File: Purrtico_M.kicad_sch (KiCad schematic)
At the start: 119 parts, among them J1 Conn_02x05_Odd_Even, J2 Conn_01x02, J4 Conn_01x02, U1 OPA1679, U2 OPA1679, U3 OPA1679

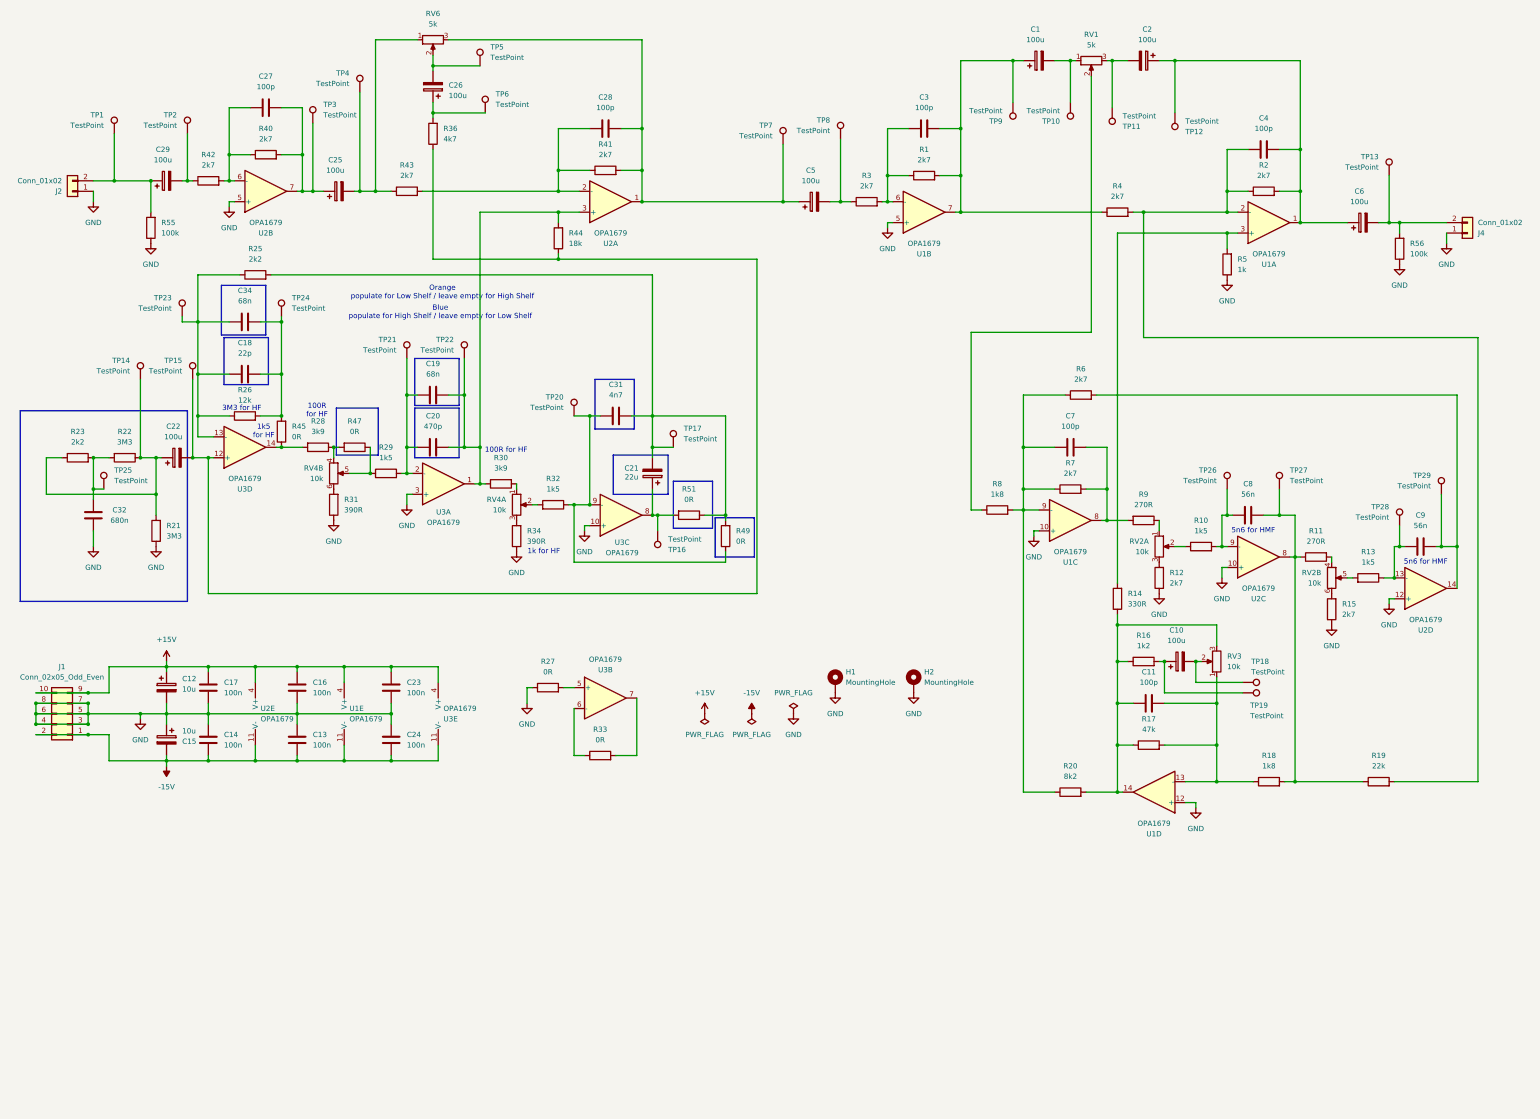
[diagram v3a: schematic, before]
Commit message: update pcb
swapped potentiometer pinouts, increased potentiometer spacing on pcb
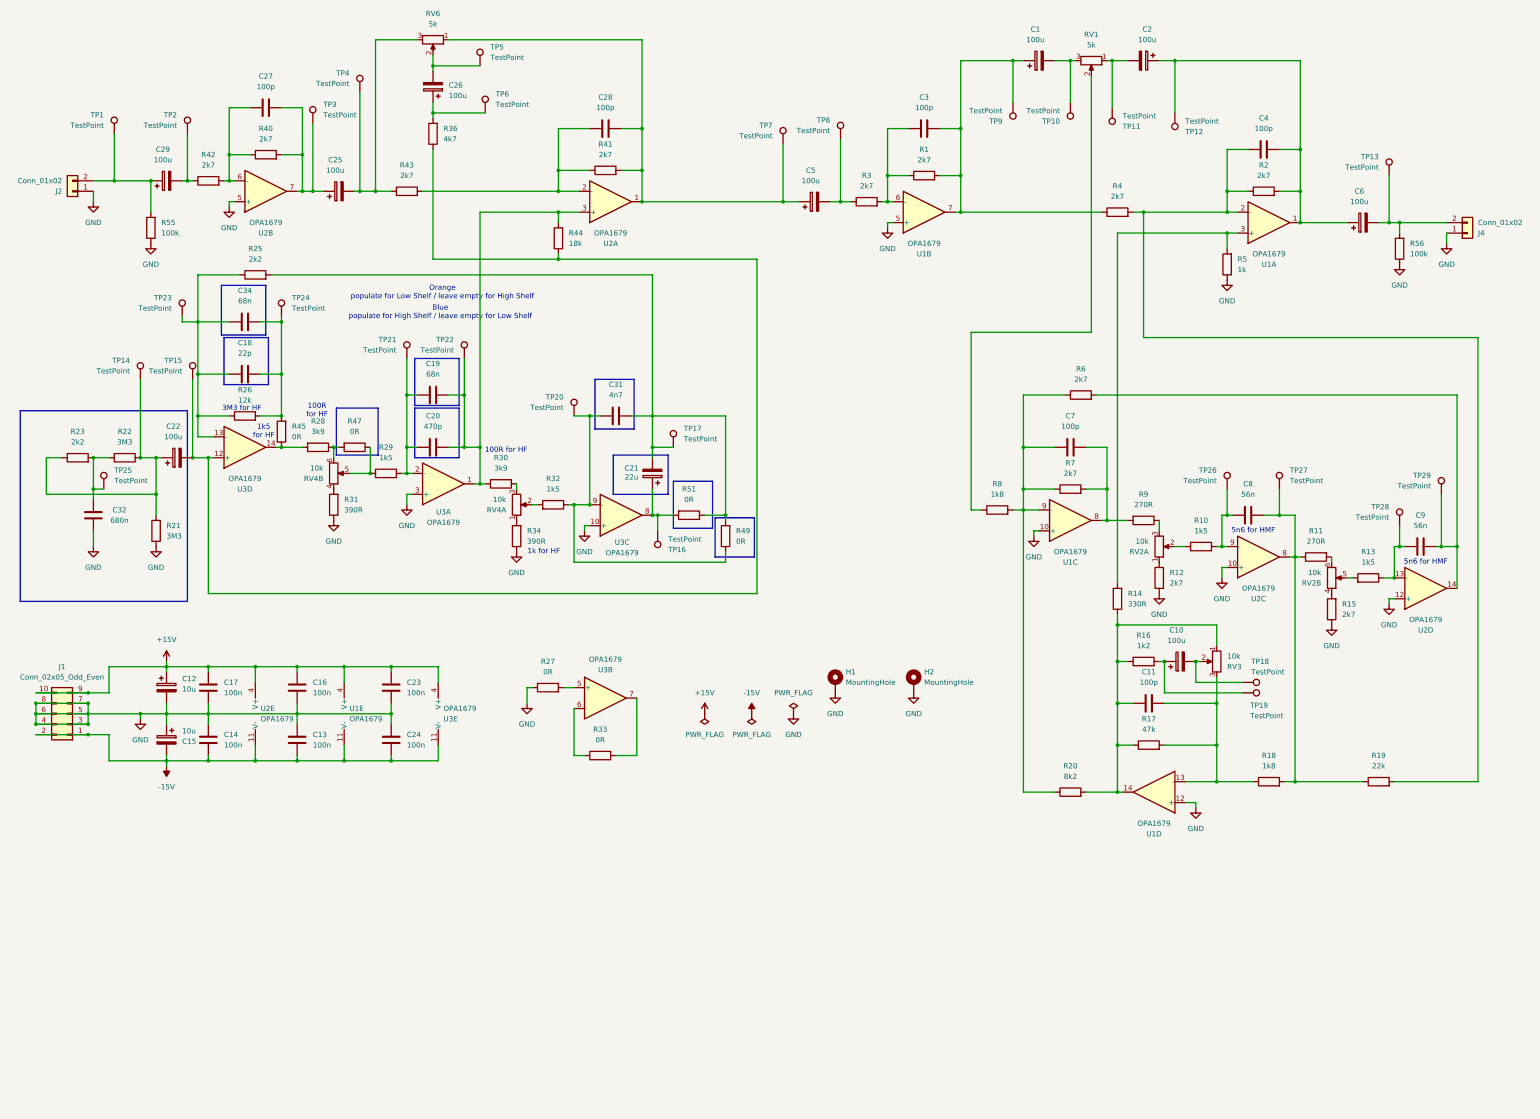
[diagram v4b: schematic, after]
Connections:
- net at C1.2, TP10.1: now also RV1.3; no longer RV1.1
- net at C2.2, TP11.1: now also RV1.1; no longer RV1.3
- net at C25.2, R43.1, TP4.1: now also RV6.3; no longer RV6.1
- net at C28.2, C5.1, R41.2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: now also RV6.1; no longer RV6.3
- net at C11.1, R14.1, R16.1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: now also RV3.1; no longer RV3.3
- net at C11.2, R17.2, R18.1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: now also RV3.3; no longer RV3.1
- net at R9.1: now also RV2.3; no longer RV2.1
- net at R28.1, R47.2: now also RV4.6; no longer RV4.4
- net at R31.2: now also RV4.4; no longer RV4.6
- net at R11.2: now also RV2.6; no longer RV2.4
- net at R12.2: now also RV2.1; no longer RV2.3
- net at R15.2: now also RV2.4; no longer RV2.6
- net at R34.2: now also RV4.1; no longer RV4.3
- net at R30.2: now also RV4.3; no longer RV4.1
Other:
- moved on the sheet: RV1, RV3, RV6
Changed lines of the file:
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@@
 	(symbol
 		(lib_id "Device:R_Potentiometer")
-		(at 295.91 27.94 90)
-		(mirror x)
+		(at 295.91 27.94 270)
 		(unit 1)
 		(exclude_from_sim no)
@@
 		(on_board yes)
 		(dnp no)
-		(fields_autoplaced yes)
 		(property "Reference" "RV1"
 			(at 295.91 21.59 90)
@@
 	(symbol
 		(lib_id "Device:R_Potentiometer")
-		(at 135.89 22.86 90)
-		(mirror x)
+		(at 135.89 22.86 270)
 		(unit 1)
 		(exclude_from_sim no)
@@
 		(on_board yes)
 		(dnp no)
-		(fields_autoplaced yes)
 		(property "Reference" "RV6"
 			(at 135.89 16.51 90)
@@
 		(lib_id "Device:R_Potentiometer_Dual_Separate")
 		(at 111.76 128.27 0)
+		(mirror x)
 		(unit 2)
 		(exclude_from_sim no)
@@
 		(dnp no)
 		(property "Reference" "RV4"
-			(at 109.22 126.9999 0)
+			(at 109.22 129.5401 0)
 			(effects
 				(font
@@
 		)
 		(property "Value" "10k"
-			(at 109.22 129.5399 0)
+			(at 109.22 127.0001 0)
 			(effects
 				(font
@@
 		(lib_id "Device:R_Potentiometer_Dual_Separate")
 		(at 312.42 146.05 0)
+		(mirror x)
 		(unit 1)
 		(exclude_from_sim no)
@@
 		(on_board yes)
 		(dnp no)
-		(fields_autoplaced yes)
 		(property "Reference" "RV2"
-			(at 309.88 144.7799 0)
+			(at 309.88 147.3201 0)
 			(effects
 				(font
@@
 		)
 		(property "Value" "10k"
-			(at 309.88 147.3199 0)
+			(at 309.88 144.7801 0)
 			(effects
 				(font
@@
 		(lib_id "Device:R_Potentiometer_Dual_Separate")
 		(at 354.33 153.67 0)
+		(mirror x)
 		(unit 2)
 		(exclude_from_sim no)
@@
 		(dnp no)
 		(property "Reference" "RV2"
-			(at 351.79 152.3999 0)
+			(at 351.79 154.9401 0)
 			(effects
 				(font
@@
 		)
 		(property "Value" "10k"
-			(at 351.79 154.9399 0)
+			(at 351.79 152.4001 0)
 			(effects
 				(font
@@
 		(lib_id "Device:R_Potentiometer_Dual_Separate")
 		(at 156.21 135.89 0)
+		(mirror x)
 		(unit 1)
 		(exclude_from_sim no)
@@
 		(on_board yes)
 		(dnp no)
-		(fields_autoplaced yes)
 		(property "Reference" "RV4"
-			(at 153.67 134.6199 0)
+			(at 153.67 137.1601 0)
 			(effects
 				(font
@@
 		)
 		(property "Value" "10k"
-			(at 153.67 137.1599 0)
+			(at 153.67 134.6201 0)
 			(effects
 				(font
@@
 	(symbol
 		(lib_id "Device:R_Potentiometer")
-		(at 326.39 173.99 180)
+		(at 326.39 173.99 0)
+		(mirror y)
 		(unit 1)
 		(exclude_from_sim no)
@@
 		(on_board yes)
 		(dnp no)
-		(fields_autoplaced yes)
 		(property "Reference" "RV3"
-			(at 328.93 172.7199 0)
+			(at 328.93 175.2601 0)
 			(effects
 				(font
@@
 		)
 		(property "Value" "10k"
-			(at 328.93 175.2599 0)
+			(at 328.93 172.7201 0)
 			(effects
 				(font

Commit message: clean up pcb
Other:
- title: Purrtico M EQ -> Purrtico M
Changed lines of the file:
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@@
 	(paper "A3")
 	(title_block
-		(title "Purrtico M EQ")
-		(date "2024-07-31")
+		(title "Purrtico M")
+		(date "2024-08-02")
 		(rev "01")
 		(company "Greybox Audio")

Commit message: tweak LF EQ
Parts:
- C19: value 68n -> 100n
- C32: value 680n -> 1u
- R23: value 2k2 -> 1k
- R28, R30: value 3k9 -> 100R
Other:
- note removed: "100R for HF"
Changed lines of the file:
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@@
 	(title_block
 		(title "Purrtico M")
-		(date "2024-08-02")
+		(date "2024-08-03")
 		(rev "01")
 		(company "Greybox Audio")
@@
 		)
 	)
-	(text "100R for HF"
-		(exclude_from_sim no)
-		(at 153.67 122.682 0)
-		(effects
-			(font
-				(size 1.27 1.27)
-			)
-		)
-	)
 	(text "5n6 for HMF"
 		(exclude_from_sim no)
@@
 		)
 	)
-	(text "100R\nfor HF"
-		(exclude_from_sim no)
-		(at 107.696 113.03 0)
-		(effects
-			(font
-				(size 1.27 1.27)
-			)
-		)
-	)
 	(text "1k5\nfor HF"
 		(exclude_from_sim no)
@@
 			)
 		)
-		(property "Value" "68n"
+		(property "Value" "100n"
 			(at 135.89 104.14 90)
 			(effects
@@
 			)
 		)
-		(property "Value" "680n"
+		(property "Value" "1u"
 			(at 59.69 139.7 0)
 			(effects
@@
 			)
 		)
-		(property "Value" "3k9"
+		(property "Value" "100R"
 			(at 107.95 118.11 90)
 			(effects
@@
 			)
 		)
-		(property "Value" "2k2"
+		(property "Value" "1k"
 			(at 49.53 120.65 90)
 			(effects
@@
 			)
 		)
-		(property "Value" "3k9"
+		(property "Value" "100R"
 			(at 152.4 127 90)
 			(effects

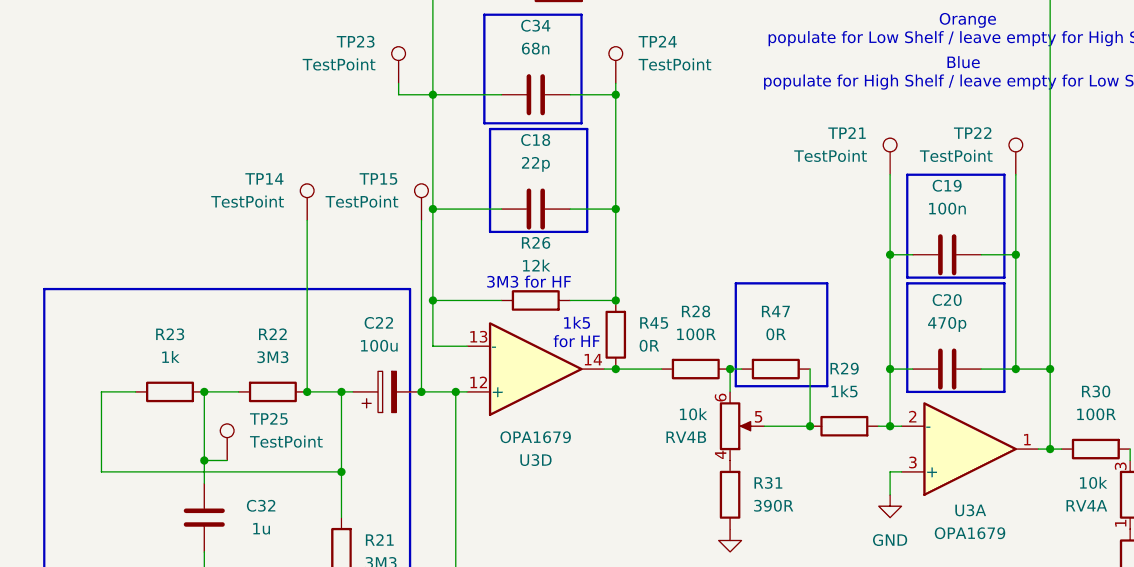
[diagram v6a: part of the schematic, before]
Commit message: tuned low shelf
tuned the low shelf so that it closely matches the 5033
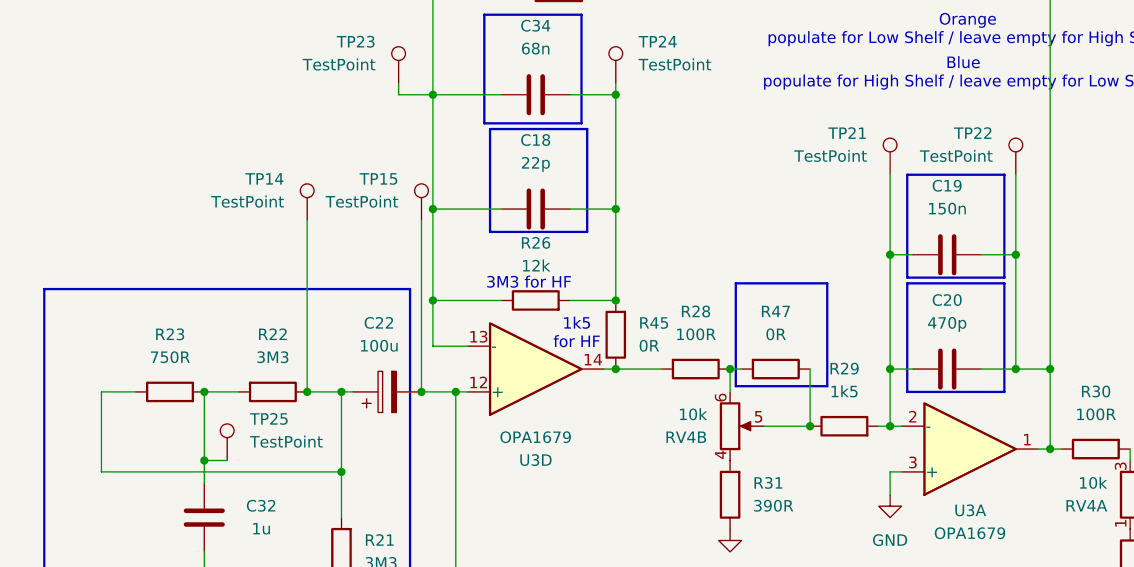
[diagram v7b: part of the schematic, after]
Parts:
- C19: value 100n -> 150n
- R23: value 1k -> 750R
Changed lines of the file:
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@@
 	(title_block
 		(title "Purrtico M")
-		(date "2024-08-03")
+		(date "2024-08-05")
 		(rev "01")
 		(company "Greybox Audio")
@@
 			)
 		)
-		(property "Value" "100n"
+		(property "Value" "150n"
 			(at 135.89 104.14 90)
 			(effects
@@
 			)
 		)
-		(property "Value" "1k"
+		(property "Value" "750R"
 			(at 49.53 120.65 90)
 			(effects

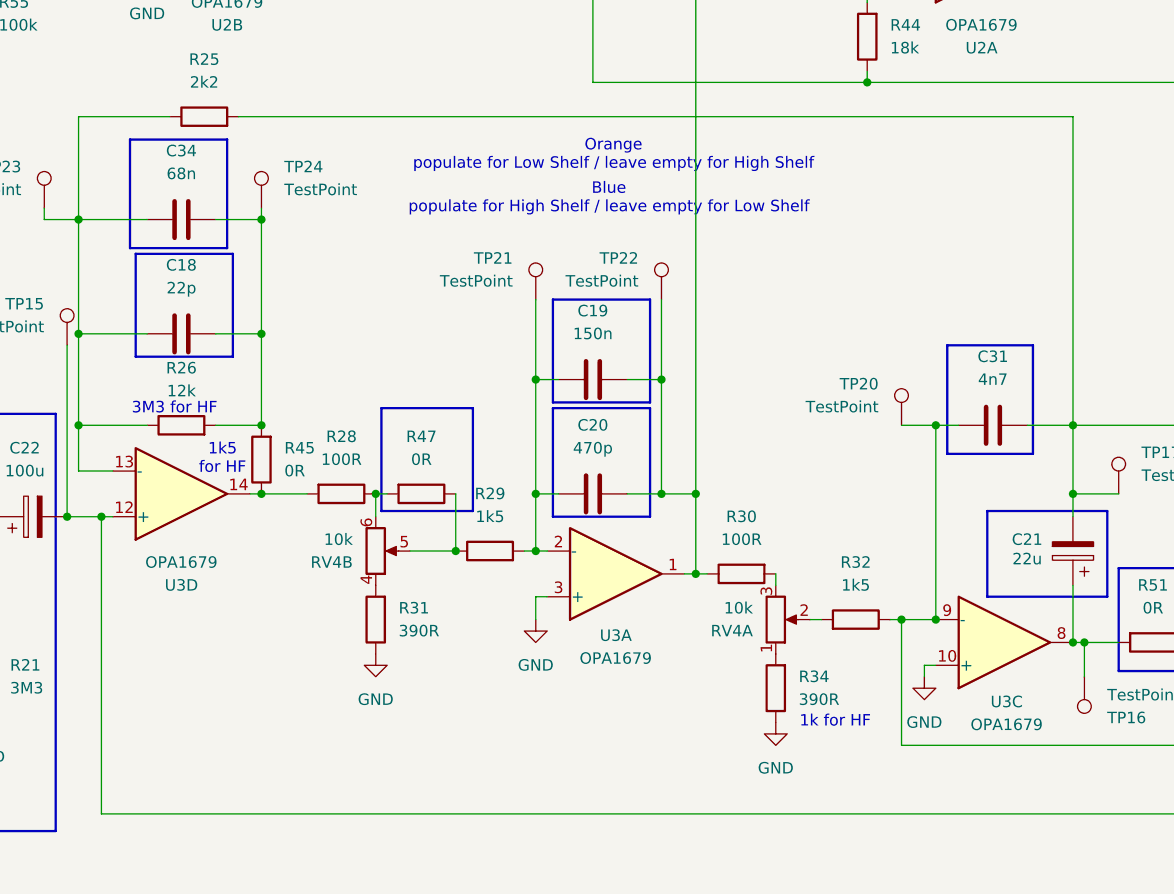
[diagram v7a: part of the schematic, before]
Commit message: update high shelf
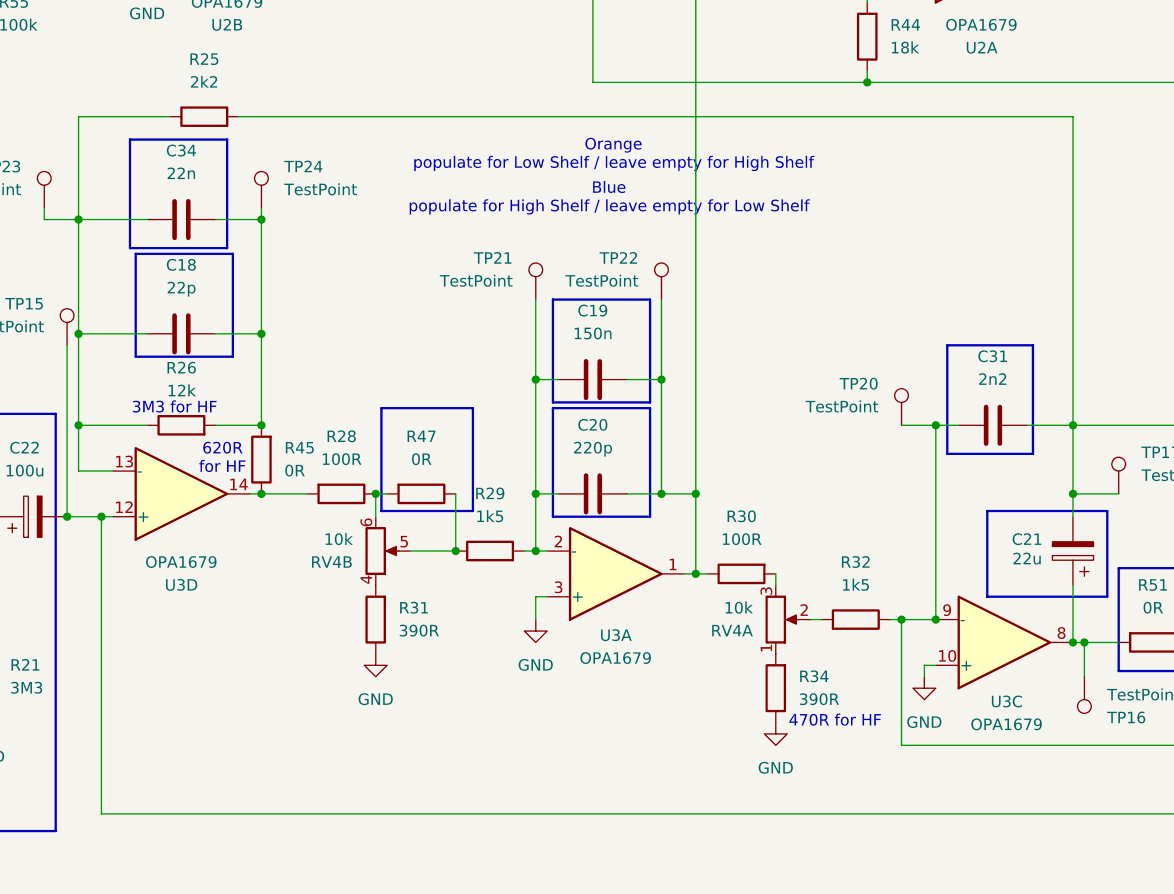
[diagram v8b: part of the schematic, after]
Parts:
- C20: value 470p -> 220p
- C31: value 4n7 -> 2n2
- C34: value 68n -> 22n
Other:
- note added: "470R for HF"
- note added: "620R for HF"
- note removed: "1k for HF"
- note removed: "1k5 for HF"
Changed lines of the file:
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@@
 			(width 0.254)
 			(type solid)
-			(color 0 194 194 1)
+			(color 0 0 194 1)
 		)
 		(fill
@@
 			(width 0.254)
 			(type solid)
-			(color 0 194 194 1)
+			(color 0 0 194 1)
 		)
 		(fill
@@
 			(width 0.254)
 			(type solid)
-			(color 0 194 194 1)
+			(color 0 0 194 1)
 		)
 		(fill
@@
 			(width 0.254)
 			(type solid)
-			(color 0 194 194 1)
+			(color 0 0 194 1)
 		)
 		(fill
@@
 			(width 0.254)
 			(type solid)
-			(color 0 194 194 1)
+			(color 0 0 194 1)
 		)
 		(fill
@@
 		)
 	)
-	(text "1k for HF"
+	(text "470R for HF"
 		(exclude_from_sim no)
 		(at 162.814 147.32 0)
@@
 		)
 	)
-	(text "1k5\nfor HF"
+	(text "620R\nfor HF"
 		(exclude_from_sim no)
 		(at 94.742 118.11 0)
@@
 			)
 		)
-		(property "Value" "4n7"
+		(property "Value" "2n2"
 			(at 180.34 109.22 90)
 			(effects
@@
 			)
 		)
-		(property "Value" "470p"
+		(property "Value" "220p"
 			(at 135.89 116.84 90)
 			(effects
@@
 			)
 		)
-		(property "Value" "68n"
+		(property "Value" "22n"
 			(at 90.17 86.36 90)
 			(effects
